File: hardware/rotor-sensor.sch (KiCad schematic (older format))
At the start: 26 parts, among them J1 Conn_01x03, J2 Conn_01x03, J3 Conn_01x03, U1 ATtiny202-SS, U2 EE-SX1081, U3 SM351LT

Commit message: Second hardware iteration
Cleaned up the schematic and reworked the entire PCB.
Replaced EE-SX1083 with EE-SX199, added 3D model and new component.
Added modified worksheet so that the PCB origin can be 0, 0.
Added scripts to execute certain tasks locally and updated the workflow accordingly.
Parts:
- removed TP1, TP2, TP3, TP4, TP5, TP6: TestPoint_Alt, TestPoint:TestPoint_Pad_D1.0mm, symbol Connector:TestPoint_Alt
- removed U2: EE-SX1081, local:EE-SX1081, symbol local:EE-SX1081
- added TP1: +, TestPoint:TestPoint_Pad_D1.0mm, symbol Connector:TestPoint_Small
- added TP10: AC-, TestPoint:TestPoint_Pad_D1.0mm, symbol Connector:TestPoint_Small
- added TP11: AC+, TestPoint:TestPoint_Pad_D1.0mm, symbol Connector:TestPoint_Small
- added TP12: IN, TestPoint:TestPoint_Pad_D1.0mm, symbol Connector:TestPoint_Small
- added TP13: OUT, TestPoint:TestPoint_Pad_D1.0mm, symbol Connector:TestPoint_Small
- added TP2, TP7: COM, TestPoint:TestPoint_Pad_D1.0mm, symbol Connector:TestPoint_Small
- added TP3: VD, TestPoint:TestPoint_Pad_D1.0mm, symbol Connector:TestPoint_Small
- added TP4: VCC, TestPoint:TestPoint_Pad_D1.0mm, symbol Connector:TestPoint_Small
- added TP5: -, TestPoint:TestPoint_Pad_D1.0mm, symbol Connector:TestPoint_Small
- added TP6: UPDI, TestPoint:TestPoint_Pad_D1.0mm, symbol Connector:TestPoint_Small
- added TP8: W2, TestPoint:TestPoint_Pad_D1.0mm, symbol Connector:TestPoint_Small
- added TP9: SENSE, TestPoint:TestPoint_Pad_D1.0mm, symbol Connector:TestPoint_Small
- added U2: EE-SX199, local:EE-SX199, symbol local:EE-SX199
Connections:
- net labels added: OS_INPUT, OS_OUTPUT, PA0_UPDI
- wire segments 60 -> 68
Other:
- note added: "EXTERNAL SENSOR\nCONNECTOR"
- note added: "EXTERNAL VOLTAGE\nREFERENCE"
- note added: "ONBOARD\nHALL SENSOR"
- note added: "ONBOARD\nOPTICAL SENSOR"
- note removed: "ONBOARD PERIPHERALS"
- moved on the sheet: C1, C2, C3, D1, D2, D3, J1, J2, J3, L1, R1, R2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

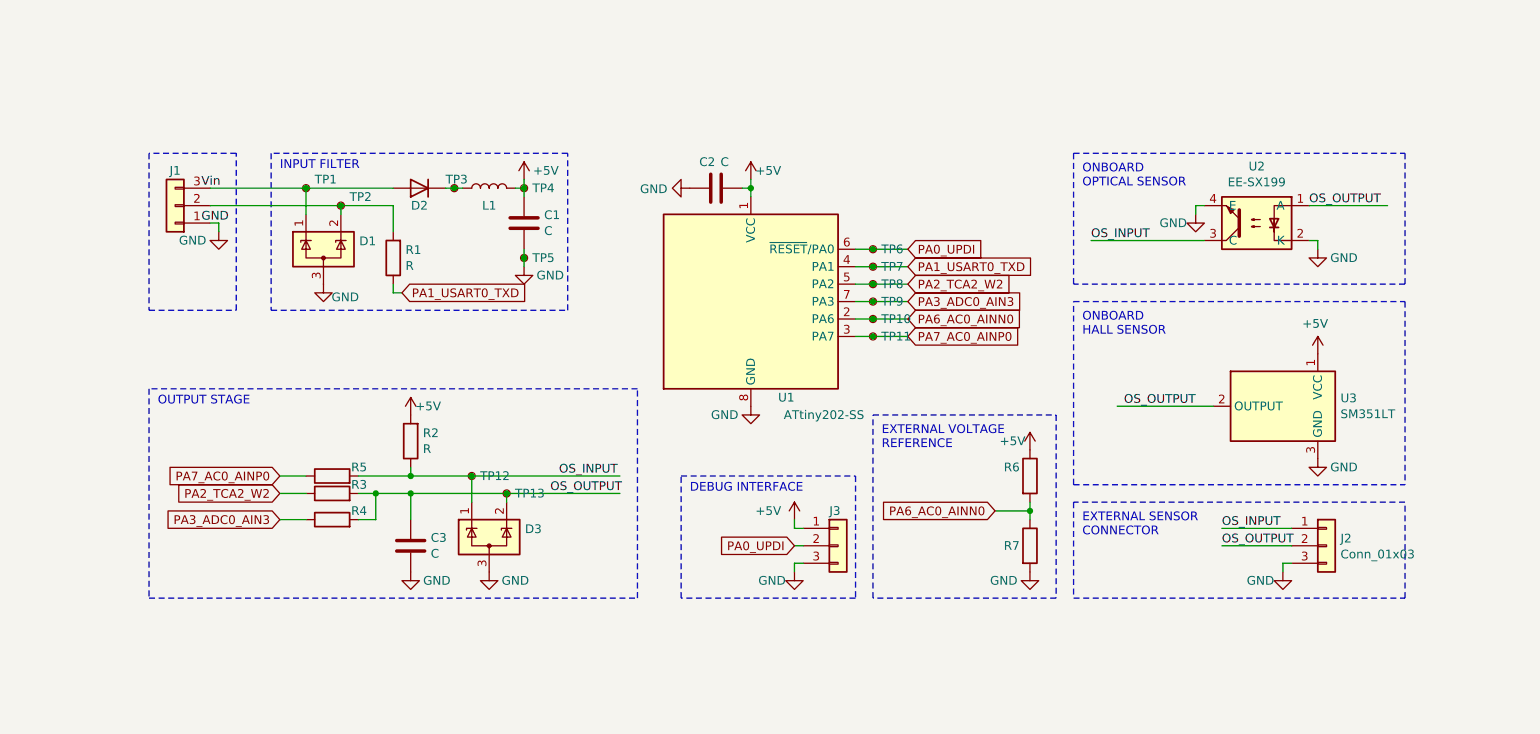
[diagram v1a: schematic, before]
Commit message: Consolidates workflow execution
Workflow now runs for the different variants.
The KiBot configuration has been merged into a single file.
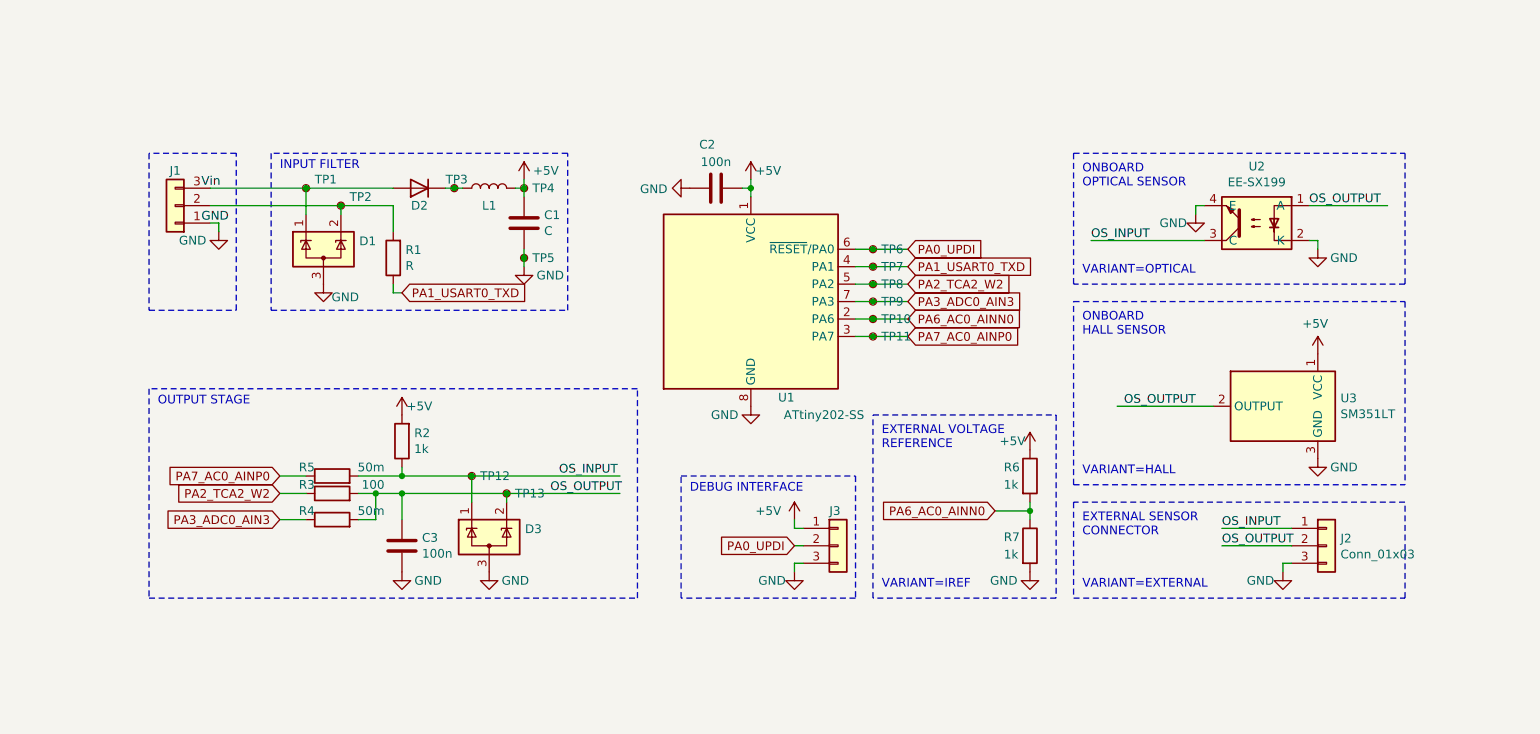
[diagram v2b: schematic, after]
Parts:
- C2, C3: value C -> 100n
- J2: Config (none) -> +EXTERNAL
- R2: value R -> 1k
- R3: value R -> 100
- R4, R5: value R -> 50m
- R6, R7: value R -> 1k; Config (none) -> +IREF
- TP2: value COM -> COMA
- TP7: value COM -> COMB
- U2: Config (none) -> +OPTICAL
- U3: Config (none) -> +HALL
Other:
- note added: "VARIANT=EXTERNAL"
- note added: "VARIANT=HALL"
- note added: "VARIANT=IREF"
- note added: "VARIANT=OPTICAL"
- moved on the sheet: C3, R2
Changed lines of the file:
@@
 L Device:R R2
 U 1 1 61227B72
-P 3850 4200
-F 0 "R2" H 3780 4154 50  0000 R CNN
-F 1 "R" H 3780 4245 50  0000 R CNN
-F 2 "Resistor_SMD:R_0603_1608Metric" V 3780 4200 50  0001 C CNN
-F 3 "~" H 3850 4200 50  0001 C CNN
-	1    3850 4200
+P 3800 4200
+F 0 "R2" H 3730 4154 50  0000 R CNN
+F 1 "1k" H 3730 4245 50  0000 R CNN
+F 2 "Resistor_SMD:R_0603_1608Metric" V 3730 4200 50  0001 C CNN
+F 3 "~" H 3800 4200 50  0001 C CNN
+	1    3800 4200
 	-1   0    0    1
 $EndComp
@@
 U 1 1 6122E61F
 P 3400 4500
-F 0 "R3" V 3450 4300 50  0000 L CNN
-F 1 "R" H 3470 4455 50  0001 L CNN
+F 0 "R3" V 3450 4600 50  0000 L CNN
+F 1 "100" V 3450 4200 50  0000 L CNN
 F 2 "Resistor_SMD:R_0603_1608Metric" V 3330 4500 50  0001 C CNN
 F 3 "~" H 3400 4500 50  0001 C CNN
@@
 F 2 "Connector_PinHeader_2.54mm:PinHeader_1x03_P2.54mm_Vertical" H 9100 4800 50  0001 C CNN
 F 3 "~" H 9100 4800 50  0001 C CNN
+F 4 "+EXTERNAL" H 9100 4800 50  0001 C CNN "Config"
 	1    9100 4800
 	1    0    0    -1
@@
 U 1 1 612593EC
 P 5600 2750
-F 0 "C2" V 5450 2700 50  0000 C CNN
-F 1 "C" V 5450 2800 50  0000 C CNN
+F 0 "C2" V 5350 2700 50  0000 C CNN
+F 1 "100n" V 5450 2750 50  0000 C CNN
 F 2 "Capacitor_SMD:C_0603_1608Metric" H 5638 2600 50  0001 C CNN
 F 3 "~" H 5600 2750 50  0001 C CNN
@@
 L power:+5V #PWR010
 U 1 1 6127B6F1
-P 3850 4050
-F 0 "#PWR010" H 3850 3900 50  0001 C CNN
-F 1 "+5V" H 3950 4100 50  0000 C CNN
-F 2 "" H 3850 4050 50  0001 C CNN
-F 3 "" H 3850 4050 50  0001 C CNN
-	1    3850 4050
+P 3800 4050
+F 0 "#PWR010" H 3800 3900 50  0001 C CNN
+F 1 "+5V" H 3900 4100 50  0000 C CNN
+F 2 "" H 3800 4050 50  0001 C CNN
+F 3 "" H 3800 4050 50  0001 C CNN
+	1    3800 4050
 	1    0    0    -1
 $EndComp
@@
 F 2 "Package_TO_SOT_SMD:SOT-23" H 8800 4000 50  0001 C CNN
 F 3 "https://sensing.honeywell.com/honeywell-sensing-nanopower-series-product-sheet-50095501-a-en.pdf" H 8800 4000 50  0001 C CNN
+F 4 "+HALL" H 8850 4000 50  0001 C CNN "Config"
 	1    8850 4000
 	-1   0    0    -1
@@
 $EndComp
 Wire Wire Line
-	3850 4350 3850 4400
-Wire Wire Line
-	3850 4650 3850 4500
+	3800 4350 3800 4400
+Wire Wire Line
+	3800 4650 3800 4500
 Wire Wire Line
 	3550 4500 3650 4500
@@
 U 1 1 613AE22C
 P 3400 4650
-F 0 "R4" V 3450 4450 50  0000 L CNN
-F 1 "R" H 3470 4605 50  0001 L CNN
+F 0 "R4" V 3450 4750 50  0000 L CNN
+F 1 "50m" V 3450 4350 50  0000 L CNN
 F 2 "Resistor_SMD:R_0603_1608Metric" V 3330 4650 50  0001 C CNN
 F 3 "~" H 3400 4650 50  0001 C CNN
@@
 Connection ~ 3650 4500
 Wire Wire Line
-	3650 4500 3850 4500
+	3650 4500 3800 4500
 Wire Wire Line
 	3250 4650 3100 4650
@@
 L power:GND #PWR014
 U 1 1 6127F551
-P 3850 4950
-F 0 "#PWR014" H 3850 4700 50  0001 C CNN
-F 1 "GND" H 4000 4900 50  0000 C CNN
-F 2 "" H 3850 4950 50  0001 C CNN
-F 3 "" H 3850 4950 50  0001 C CNN
-	1    3850 4950
+P 3800 4950
+F 0 "#PWR014" H 3800 4700 50  0001 C CNN
+F 1 "GND" H 3950 4900 50  0000 C CNN
+F 2 "" H 3800 4950 50  0001 C CNN
+F 3 "" H 3800 4950 50  0001 C CNN
+	1    3800 4950
 	1    0    0    -1
 $EndComp
@@
 L Device:C C3
 U 1 1 61263E24
-P 3850 4800
-F 0 "C3" H 3965 4846 50  0000 L CNN
-F 1 "C" H 3965 4755 50  0000 L CNN
-F 2 "Capacitor_SMD:C_0603_1608Metric" H 3888 4650 50  0001 C CNN
-F 3 "~" H 3850 4800 50  0001 C CNN
-	1    3850 4800
+P 3800 4800
+F 0 "C3" H 3915 4846 50  0000 L CNN
+F 1 "100n" H 3915 4755 50  0000 L CNN
+F 2 "Capacitor_SMD:C_0603_1608Metric" H 3838 4650 50  0001 C CNN
+F 3 "~" H 3800 4800 50  0001 C CNN
+	1    3800 4800
 	1    0    0    -1
 $EndComp
@@
 U 1 1 61434E80
 P 3400 4400
-F 0 "R5" V 3450 4200 50  0000 L CNN
-F 1 "R" H 3470 4355 50  0001 L CNN
+F 0 "R5" V 3450 4500 50  0000 L CNN
+F 1 "50m" V 3450 4100 50  0000 L CNN
 F 2 "Resistor_SMD:R_0603_1608Metric" V 3330 4400 50  0001 C CNN
 F 3 "~" H 3400 4400 50  0001 C CNN
@@
 $EndComp
 Wire Wire Line
-	3850 4400 3550 4400
+	3800 4400 3550 4400
 Wire Wire Line
 	3250 4400 3100 4400
@@
 P 7400 4400
 F 0 "R6" H 7250 4450 50  0000 L CNN
-F 1 "R" H 7470 4355 50  0001 L CNN
+F 1 "1k" H 7250 4350 50  0000 L CNN
 F 2 "Resistor_SMD:R_0603_1608Metric" V 7330 4400 50  0001 C CNN
 F 3 "~" H 7400 4400 50  0001 C CNN
+F 4 "+IREF" H 7400 4400 50  0001 C CNN "Config"
 	1    7400 4400
 	1    0    0    -1
@@
 U 1 1 61437C21
 P 7400 4800
-F 0 "R7" H 7250 4800 50  0000 L CNN
-F 1 "R" H 7470 4755 50  0001 L CNN
+F 0 "R7" H 7250 4850 50  0000 L CNN
+F 1 "1k" H 7250 4750 50  0000 L CNN
 F 2 "Resistor_SMD:R_0603_1608Metric" V 7330 4800 50  0001 C CNN
 F 3 "~" H 7400 4800 50  0001 C CNN
+F 4 "+IREF" H 7400 4800 50  0001 C CNN "Config"
 	1    7400 4800
 	1    0    0    -1
@@
 Wire Wire Line
 	8900 4700 8500 4700
-Connection ~ 3850 4400
+Connection ~ 3800 4400
 Wire Wire Line
 	8900 4800 8500 4800
-Connection ~ 3850 4500
+Connection ~ 3800 4500
 Wire Wire Line
 	8350 2900 8350 2850
@@
 Connection ~ 4400 4500
 Wire Wire Line
-	4400 4500 3850 4500
+	4400 4500 3800 4500
 Wire Wire Line
 	4200 4550 4200 4400
 Connection ~ 4200 4400
 Wire Wire Line
-	4200 4400 3850 4400
+	4200 4400 3800 4400
 Text Label 8500 4700 0    50   ~ 0
 OS_INPUT
@@
 F 2 "local:EE-SX199" H 8500 2750 50  0001 L CIN
 F 3 "https://toshiba.semicon-storage.com/info/docget.jsp?did=10569&prodName=TLP785F" H 8700 2950 50  0001 L CNN
+F 4 "+OPTICAL" H 8700 2950 50  0001 C CNN "Config"
 	1    8700 2950
 	-1   0    0    -1
@@
 P 6500 3200
 F 0 "TP7" H 6548 3200 50  0000 L CNN
-F 1 "COM" H 6548 3155 50  0001 L CNN
+F 1 "COMB" H 6548 3155 50  0001 L CNN
 F 2 "TestPoint:TestPoint_Pad_D1.0mm" H 6700 3200 50  0001 C CNN
 F 3 "~" H 6700 3200 50  0001 C CNN
@@
 P 3450 2850
 F 0 "TP2" H 3500 2900 50  0000 L CNN
-F 1 "COM" H 3498 2805 50  0001 L CNN
+F 1 "COMA" H 3498 2805 50  0001 L CNN
 F 2 "TestPoint:TestPoint_Pad_D1.0mm" H 3650 2850 50  0001 C CNN
 F 3 "~" H 3650 2850 50  0001 C CNN
@@
 Text Notes 5450 4500 0    50   ~ 0
 DEBUG INTERFACE
+Text Notes 7700 4400 0    50   ~ 0
+VARIANT=HALL
+Text Notes 7700 5050 0    50   ~ 0
+VARIANT=EXTERNAL
+Text Notes 7700 3250 0    50   ~ 0
+VARIANT=OPTICAL
+Text Notes 6550 5050 0    50   ~ 0
+VARIANT=IREF
 $EndSCHEMATC

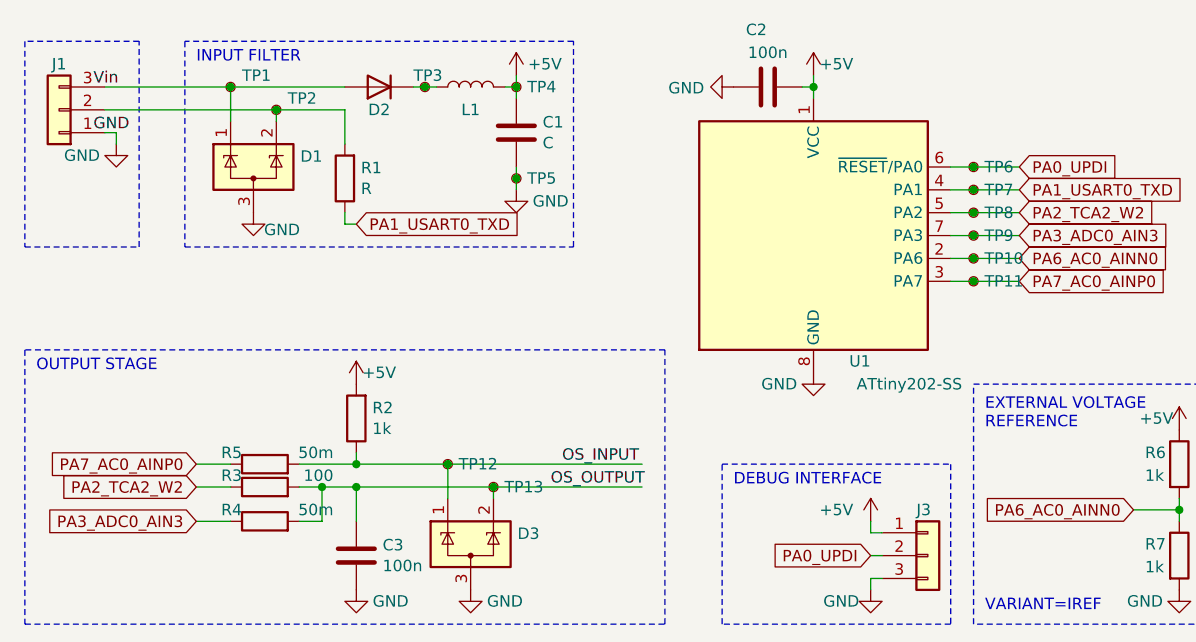
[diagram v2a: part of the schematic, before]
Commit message: Increased clearance between Slot sensor and PCB edge
Assigned component values to remaining components.
Connectors will now only be placed in the DEBUG variant
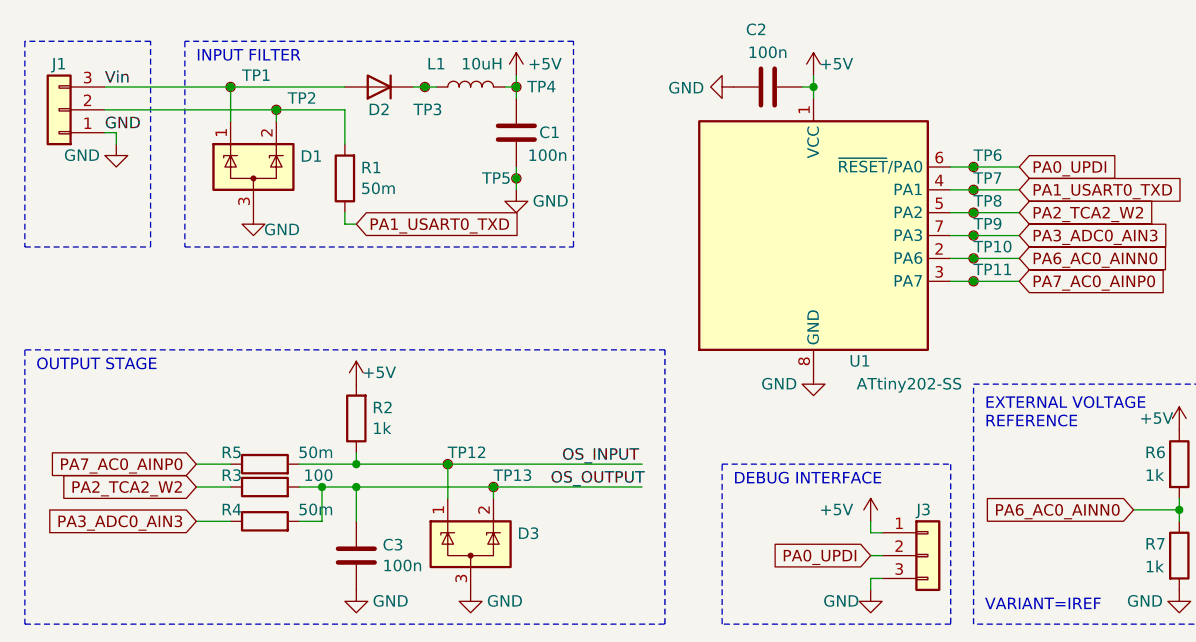
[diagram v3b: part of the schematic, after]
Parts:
- C1: value C -> 100n
- J1, J3: Config (none) -> +DEBUG
- J2: Config +EXTERNAL -> +DEBUG
- L1: value L -> 10uH
- R1: value R -> 50m
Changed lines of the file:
@@
 U 1 1 61221D8D
 P 4300 2750
-F 0 "L1" V 4200 2750 50  0000 C CNN
-F 1 "L" V 4100 2750 50  0001 C CNN
+F 0 "L1" V 4400 2900 50  0000 C CNN
+F 1 "10uH" V 4400 2700 50  0000 C CNN
 F 2 "Inductor_SMD:L_0603_1608Metric" H 4300 2750 50  0001 C CNN
 F 3 "~" H 4300 2750 50  0001 C CNN
@@
 U 1 1 61223AC4
 P 4500 2950
-F 0 "C1" H 4615 2996 50  0000 L CNN
-F 1 "C" H 4615 2905 50  0000 L CNN
+F 0 "C1" H 4600 2950 50  0000 L CNN
+F 1 "100n" H 4550 2850 50  0000 L CNN
 F 2 "Capacitor_SMD:C_0603_1608Metric" H 4538 2800 50  0001 C CNN
 F 3 "~" H 4500 2950 50  0001 C CNN
@@
 F 2 "Connector_PinHeader_2.54mm:PinHeader_1x03_P2.54mm_Vertical" H 9100 4800 50  0001 C CNN
 F 3 "~" H 9100 4800 50  0001 C CNN
-F 4 "+EXTERNAL" H 9100 4800 50  0001 C CNN "Config"
+F 4 "+DEBUG" H 9100 4800 50  0001 C CNN "Config"
 	1    9100 4800
 	1    0    0    -1
@@
 F 2 "Connector_PinHeader_2.54mm:PinHeader_1x03_P2.54mm_Vertical" H 2500 2850 50  0001 C CNN
 F 3 "~" H 2500 2850 50  0001 C CNN
+F 4 "+DEBUG" H 2500 2850 50  0001 C CNN "Config"
 	1    2500 2850
 	-1   0    0    1
@@
 P 3750 3150
 F 0 "R1" H 3680 3104 50  0000 R CNN
-F 1 "R" H 3680 3195 50  0000 R CNN
+F 1 "50m" H 3680 3195 50  0000 R CNN
 F 2 "Resistor_SMD:R_0603_1608Metric" V 3680 3150 50  0001 C CNN
 F 3 "~" H 3750 3150 50  0001 C CNN
@@
 	3750 2850 3750 3000
 Connection ~ 3450 2850
-Text Label 2650 2750 0    50   ~ 0
+Text Label 2700 2750 0    50   ~ 0
 Vin
-Text Label 2650 2950 0    50   ~ 0
+Text Label 2700 2950 0    50   ~ 0
 GND
 Wire Notes Line
@@
 F 2 "Connector_PinHeader_1.27mm:PinHeader_1x03_P1.27mm_Vertical" H 6300 4800 50  0001 C CNN
 F 3 "~" H 6300 4800 50  0001 C CNN
+F 4 "+DEBUG" H 6300 4800 50  0001 C CNN "Config"
 	1    6300 4800
 	1    0    0    -1
@@
 	7650 4450 9550 4450
 Wire Notes Line
-	2850 2550 2350 2550
+	2900 2550 2350 2550
 Wire Notes Line
 	2350 2550 2350 3450
 Wire Notes Line
-	2350 3450 2850 3450
-Wire Notes Line
-	2850 3450 2850 2550
+	2350 3450 2900 3450
+Wire Notes Line
+	2900 3450 2900 2550
 Wire Wire Line
 	4050 2750 4100 2750
@@
 U 1 1 618F2281
 P 4100 2750
-F 0 "TP3" H 4050 2800 50  0000 L CNN
+F 0 "TP3" H 4050 2650 50  0000 L CNN
 F 1 "VD" H 4148 2705 50  0001 L CNN
 F 2 "TestPoint:TestPoint_Pad_D1.0mm" H 4300 2750 50  0001 C CNN
@@
 U 1 1 618F46D6
 P 4400 4500
-F 0 "TP13" H 4448 4500 50  0000 L CNN
+F 0 "TP13" H 4400 4550 50  0000 L CNN
 F 1 "OUT" H 4448 4455 50  0001 L CNN
 F 2 "TestPoint:TestPoint_Pad_D1.0mm" H 4600 4500 50  0001 C CNN
@@
 U 1 1 618F3D8D
 P 4200 4400
-F 0 "TP12" H 4248 4400 50  0000 L CNN
+F 0 "TP12" H 4200 4450 50  0000 L CNN
 F 1 "IN" H 4248 4355 50  0001 L CNN
 F 2 "TestPoint:TestPoint_Pad_D1.0mm" H 4400 4400 50  0001 C CNN
@@
 U 1 1 618F3BD4
 P 6500 3600
-F 0 "TP11" H 6548 3600 50  0000 L CNN
+F 0 "TP11" H 6500 3650 50  0000 L CNN
 F 1 "AC+" H 6548 3555 50  0001 L CNN
 F 2 "TestPoint:TestPoint_Pad_D1.0mm" H 6700 3600 50  0001 C CNN
@@
 U 1 1 618F3A3C
 P 6500 3500
-F 0 "TP10" H 6548 3500 50  0000 L CNN
+F 0 "TP10" H 6500 3550 50  0000 L CNN
 F 1 "AC-" H 6548 3455 50  0001 L CNN
 F 2 "TestPoint:TestPoint_Pad_D1.0mm" H 6700 3500 50  0001 C CNN
@@
 U 1 1 618F3874
 P 6500 3400
-F 0 "TP9" H 6548 3400 50  0000 L CNN
+F 0 "TP9" H 6500 3450 50  0000 L CNN
 F 1 "SENSE" H 6548 3355 50  0001 L CNN
 F 2 "TestPoint:TestPoint_Pad_D1.0mm" H 6700 3400 50  0001 C CNN
@@
 U 1 1 618F3707
 P 6500 3300
-F 0 "TP8" H 6548 3300 50  0000 L CNN
+F 0 "TP8" H 6500 3350 50  0000 L CNN
 F 1 "W2" H 6548 3255 50  0001 L CNN
 F 2 "TestPoint:TestPoint_Pad_D1.0mm" H 6700 3300 50  0001 C CNN
@@
 U 1 1 618F28D3
 P 6500 3100
-F 0 "TP6" H 6548 3100 50  0000 L CNN
+F 0 "TP6" H 6500 3150 50  0000 L CNN
 F 1 "UPDI" H 6548 3055 50  0001 L CNN
 F 2 "TestPoint:TestPoint_Pad_D1.0mm" H 6700 3100 50  0001 C CNN
@@
 U 1 1 618F35DE
 P 6500 3200
-F 0 "TP7" H 6548 3200 50  0000 L CNN
+F 0 "TP7" H 6500 3250 50  0000 L CNN
 F 1 "COMB" H 6548 3155 50  0001 L CNN
 F 2 "TestPoint:TestPoint_Pad_D1.0mm" H 6700 3200 50  0001 C CNN
@@
 U 1 1 618F8E5F
 P 4500 3150
-F 0 "TP5" H 4548 3150 50  0000 L CNN
+F 0 "TP5" H 4350 3150 50  0000 L CNN
 F 1 "-" H 4548 3105 50  0001 L CNN
 F 2 "TestPoint:TestPoint_Pad_D1.0mm" H 4700 3150 50  0001 C CNN

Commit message: Panelization workflow updates
Adds fiducials to board and added tab annotation as a footprint.
Panel configuration has been updated.
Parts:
- added FID1, FID2: Fiducial, Fiducial:Fiducial_0.5mm_Mask1.5mm, symbol Mechanical:Fiducial
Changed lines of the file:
@@
 Text Notes 6550 5050 0    50   ~ 0
 VARIANT=IREF
+$Comp
+L Mechanical:Fiducial FID1
+U 1 1 61844077
+P 2600 3700
+F 0 "FID1" H 2685 3746 50  0000 L CNN
+F 1 "Fiducial" H 2685 3655 50  0000 L CNN
+F 2 "Fiducial:Fiducial_0.5mm_Mask1.5mm" H 2600 3700 50  0001 C CNN
+F 3 "~" H 2600 3700 50  0001 C CNN
+	1    2600 3700
+	1    0    0    -1
+$EndComp
+$Comp
+L Mechanical:Fiducial FID2
+U 1 1 6184520E
+P 2950 3700
+F 0 "FID2" H 3035 3746 50  0000 L CNN
+F 1 "Fiducial" H 3035 3655 50  0000 L CNN
+F 2 "Fiducial:Fiducial_0.5mm_Mask1.5mm" H 2950 3700 50  0001 C CNN
+F 3 "~" H 2950 3700 50  0001 C CNN
+	1    2950 3700
+	1    0    0    -1
+$EndComp
 $EndSCHEMATC
